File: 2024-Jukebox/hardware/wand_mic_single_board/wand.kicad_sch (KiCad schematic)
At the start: 52 parts, among them J1 USB_C_Receptacle_USB2.0, J10 Conn_01x03, J4 Conn_01x02, J6 Conn_01x01, J9 Conn_01x02, Q1 MUN5214DW1T1G, Q3 CJ3139K, U1 CP2104, U2 ESP32-PICO-D4, U3 ICM-20948, U4 TP4065-4.2V, U5 TLV76718DRVx, U6 LY68L6400SLIT, U7 PCA9306, U9 TLV76733DRVx

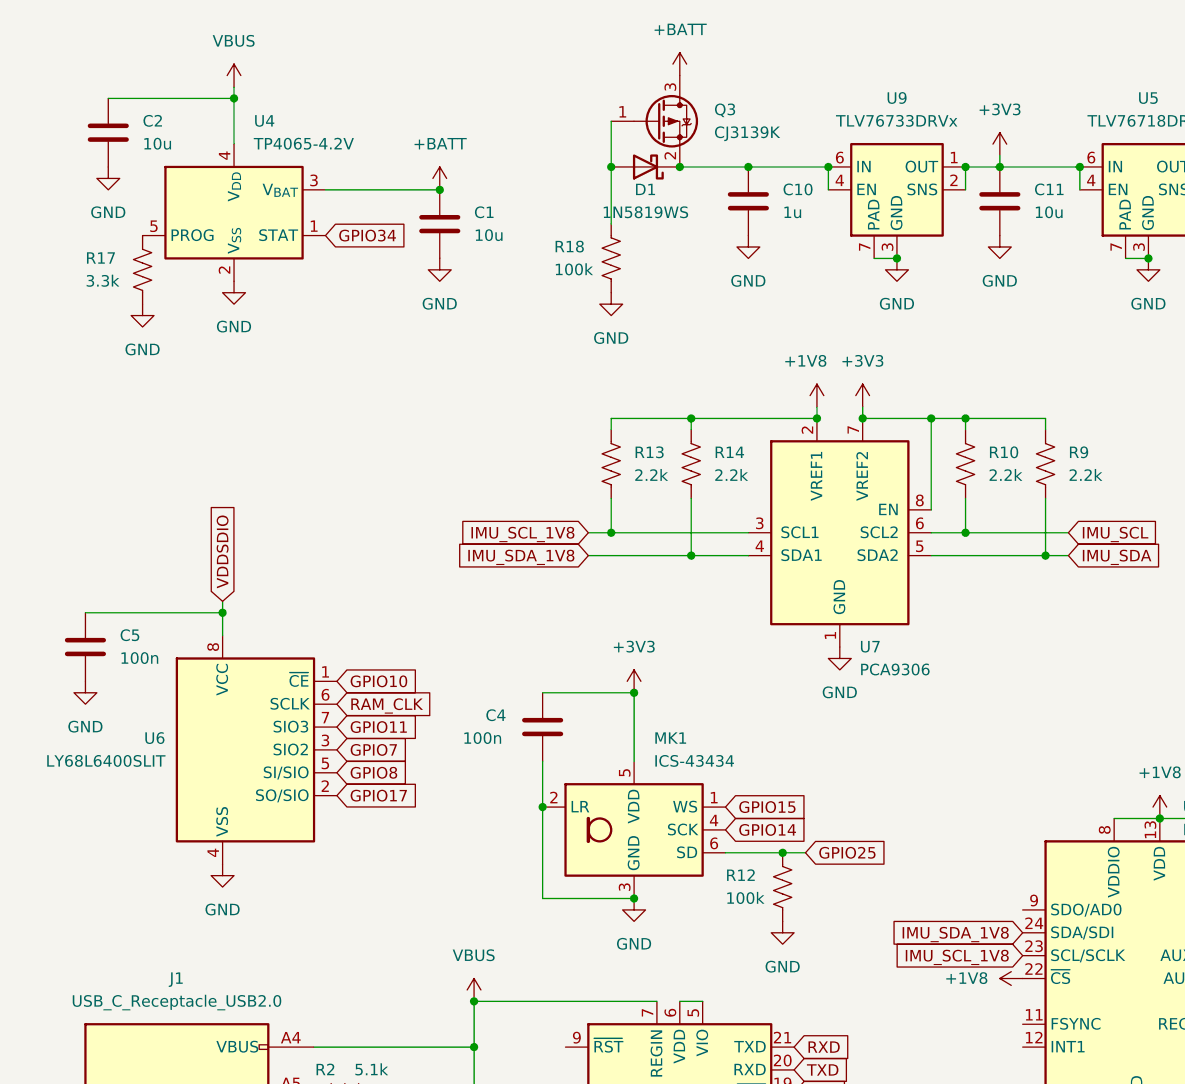
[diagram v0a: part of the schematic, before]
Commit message: Fixed wiring issue
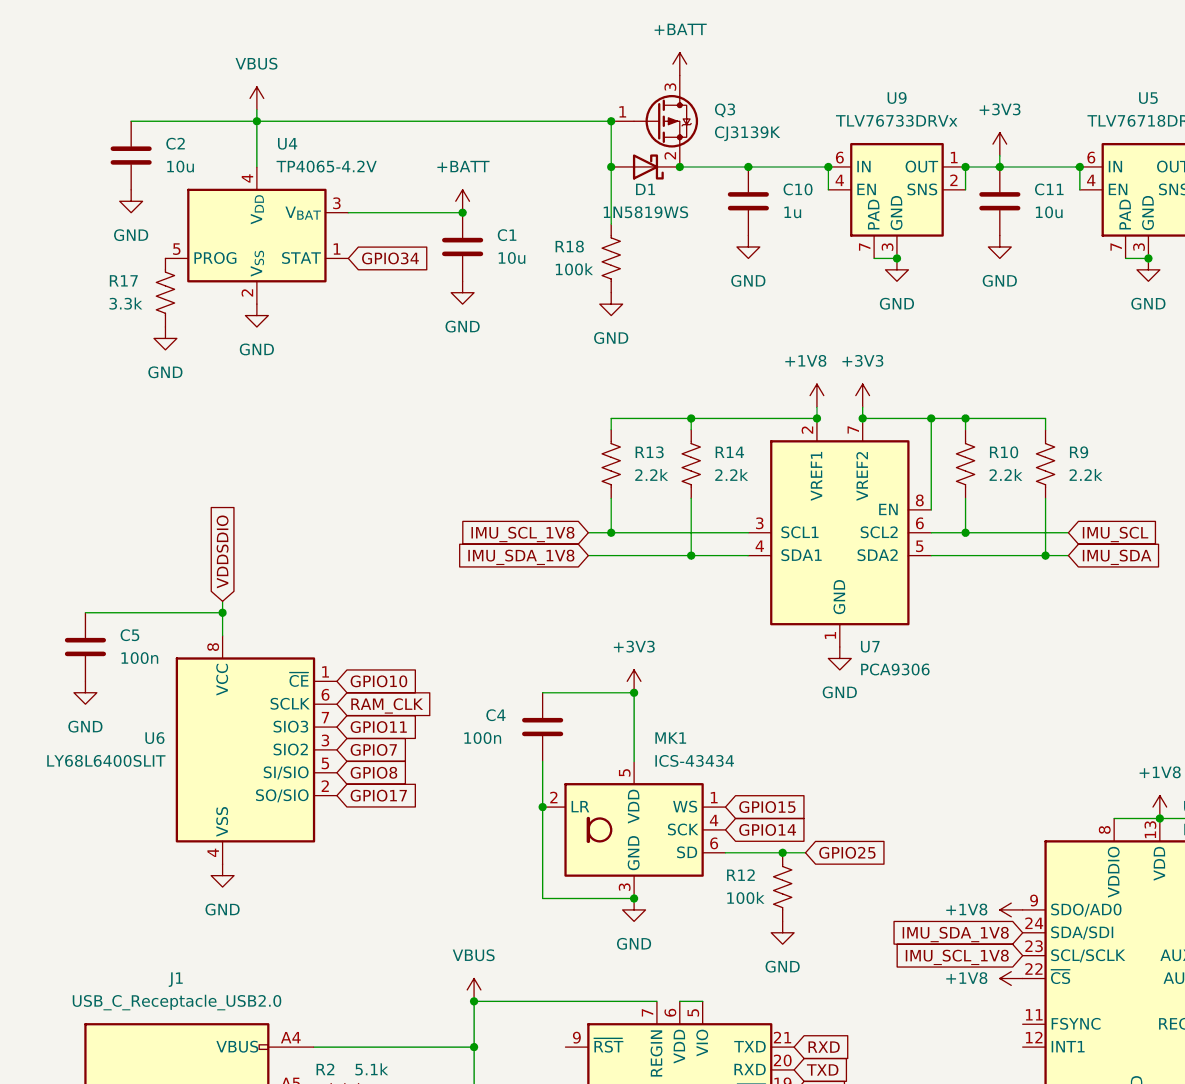
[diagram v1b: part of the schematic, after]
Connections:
- net +1V8: now also U3.9 (SDO/AD0)
- net VBUS: now also D1.2 (A), Q3.1 (G), R18.2
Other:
- moved on the sheet: C1, C2, R17, U4
